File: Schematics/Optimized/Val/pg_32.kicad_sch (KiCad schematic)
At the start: 24 parts, among them U1705 F04, U23 F04, U26 F51, U27 PA010, U30 PA011, U3602 F86, U3603 F86, U3604 F51, U3605 F74, U701 XALU32C, U703 XALU32C, U705 XVFCND, U807 XVCOND

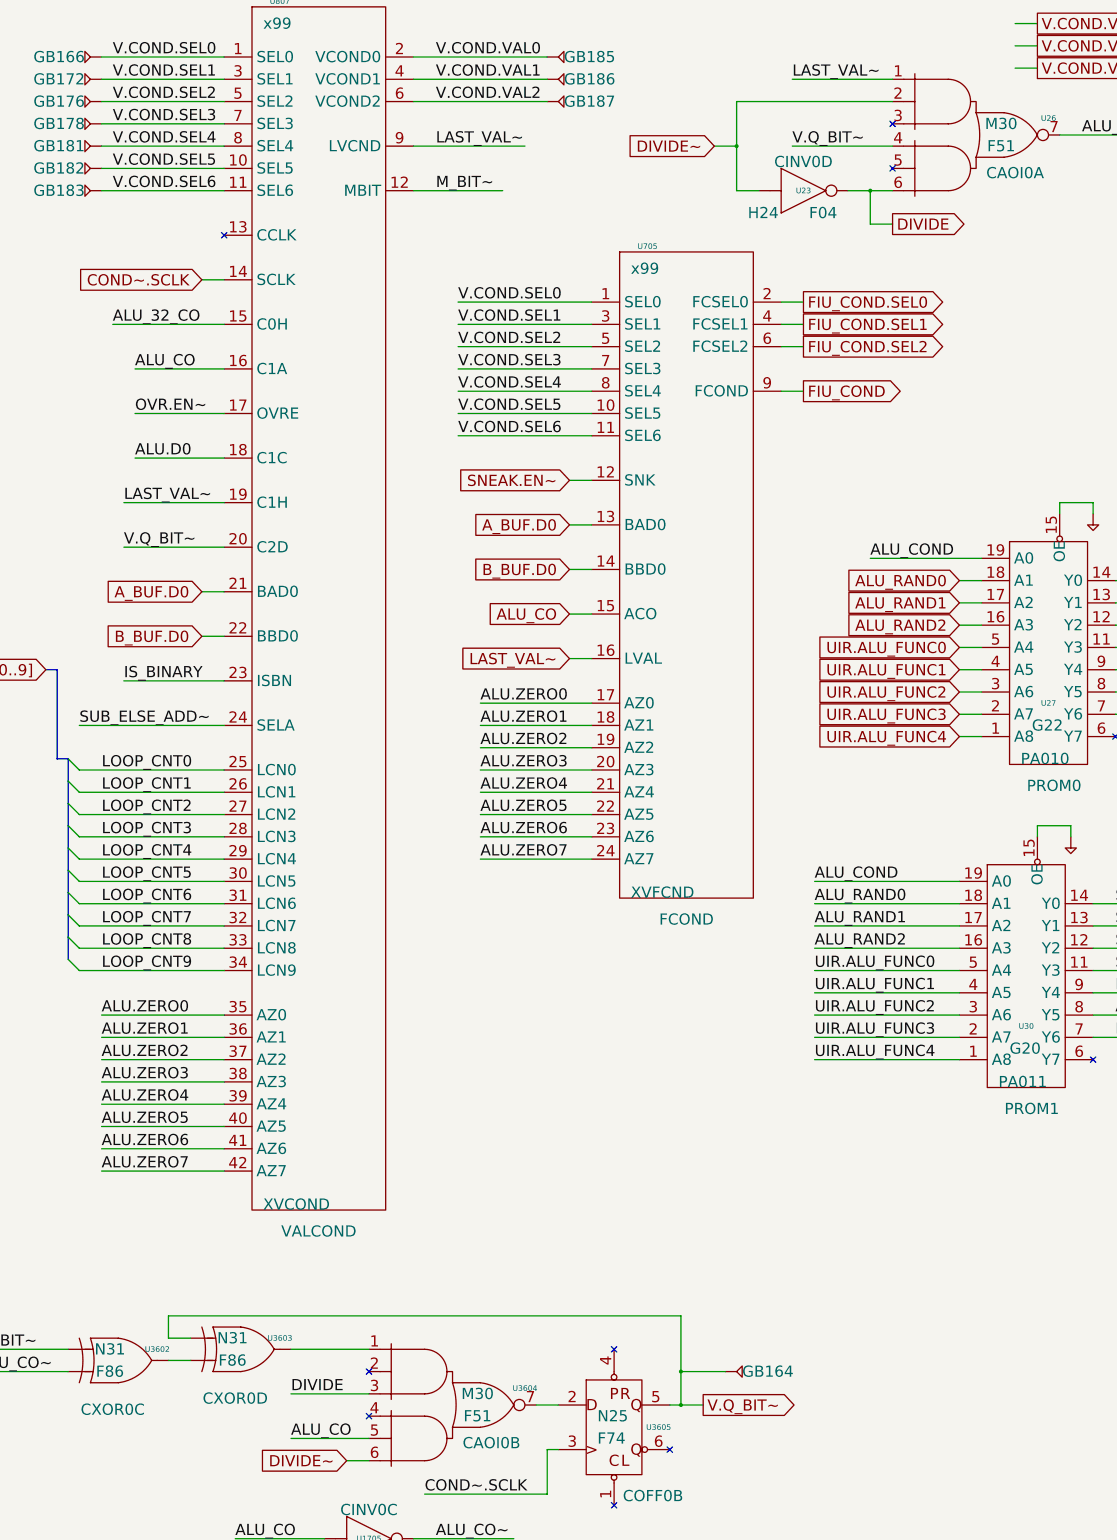
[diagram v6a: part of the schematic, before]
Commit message: Update to kicad9
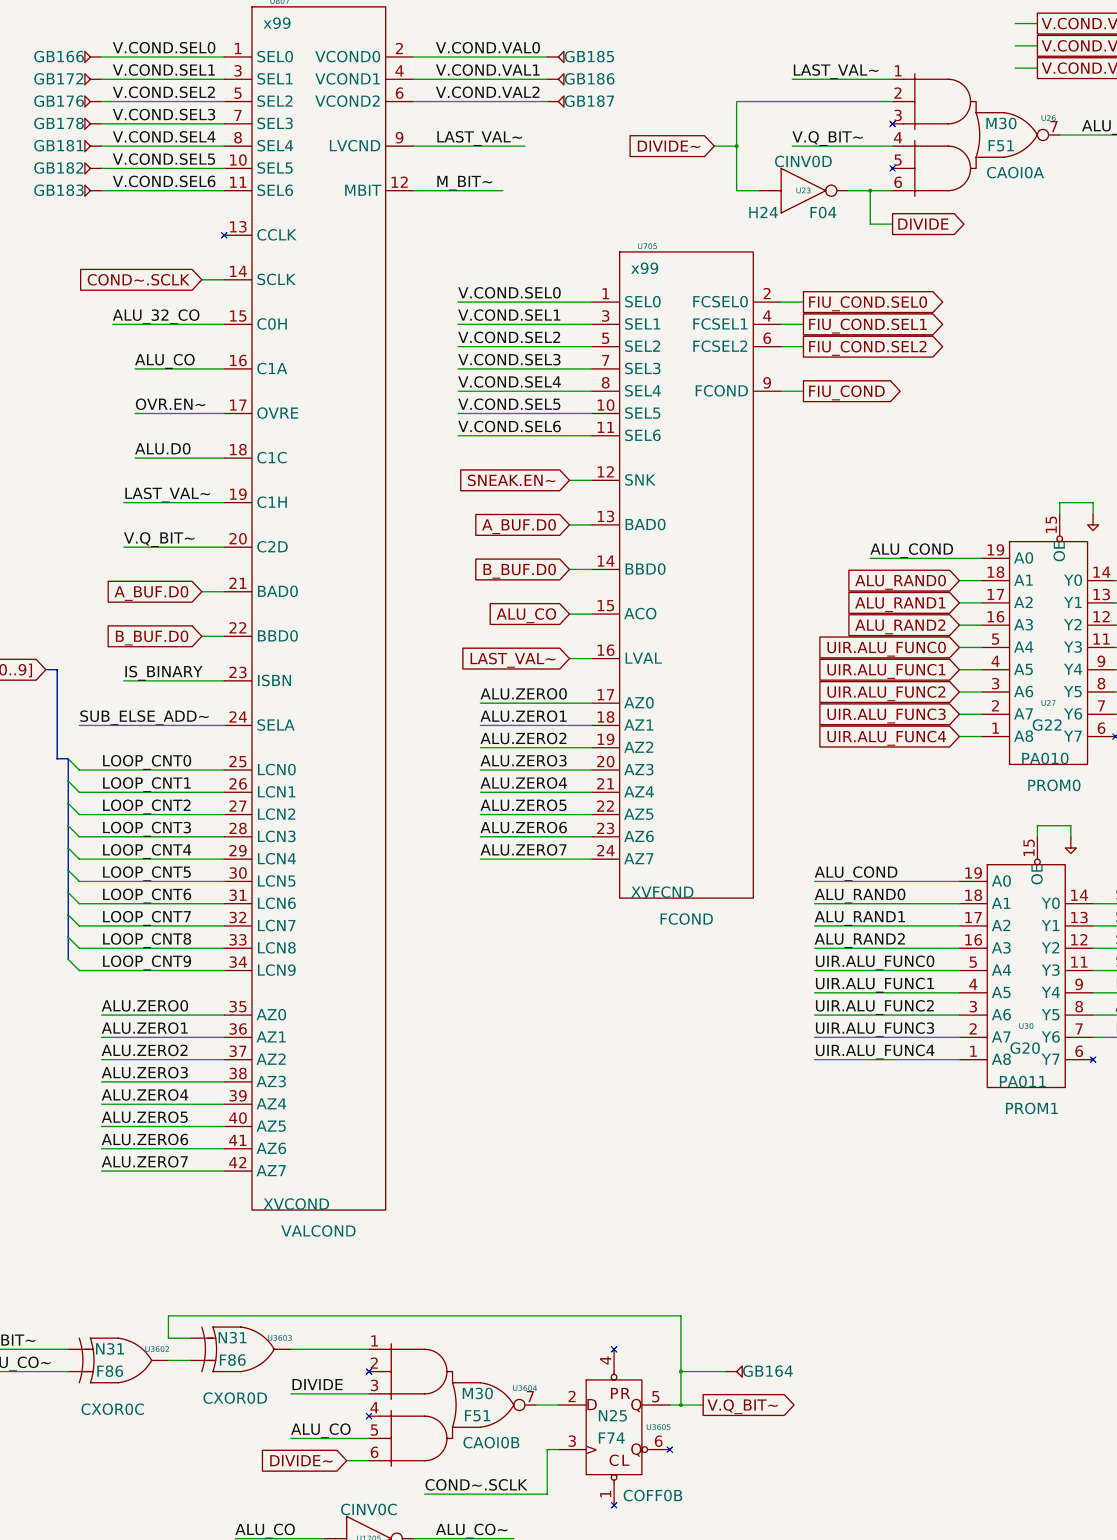
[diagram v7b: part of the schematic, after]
